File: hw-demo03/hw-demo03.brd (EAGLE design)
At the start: 83.5 x 63.5 mm, 40 parts, among them IC3 MCP2562T, IC4 STM32F042

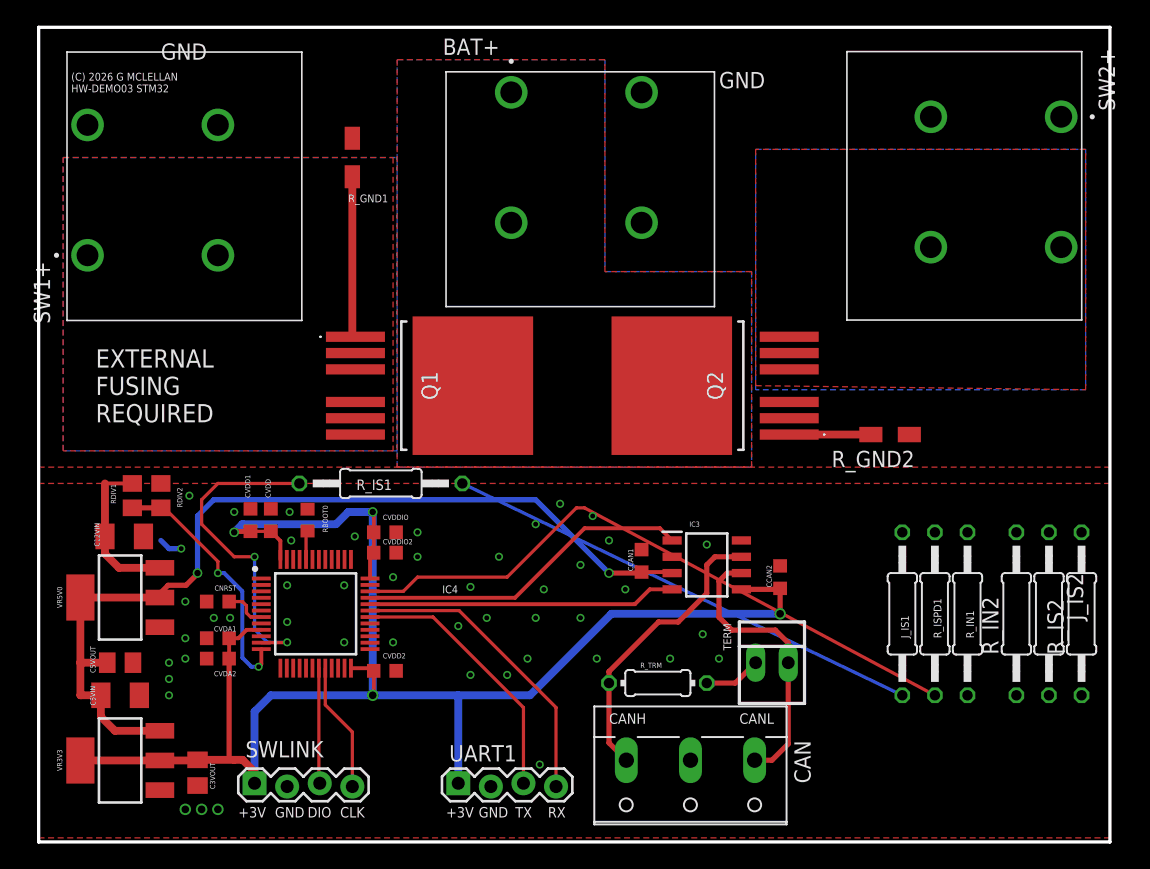
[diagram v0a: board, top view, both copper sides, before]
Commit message: first routing pass completed
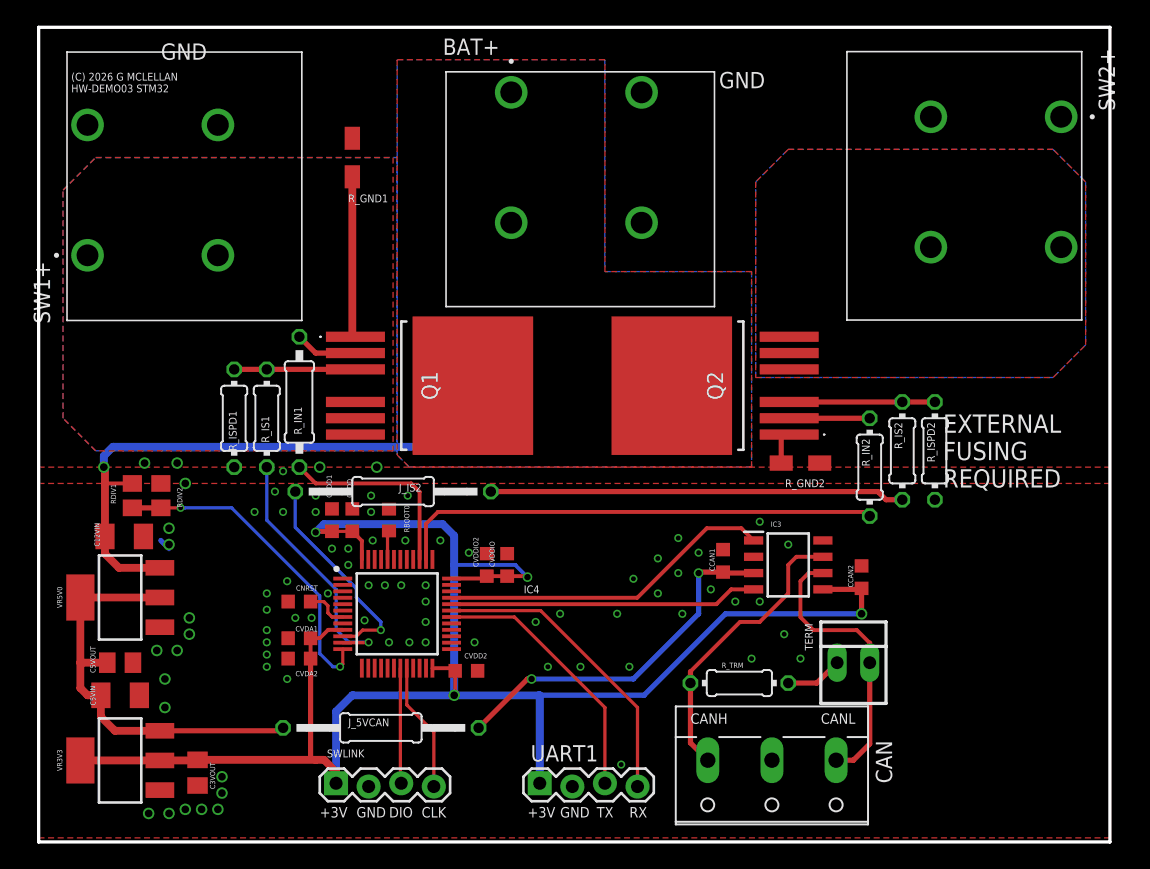
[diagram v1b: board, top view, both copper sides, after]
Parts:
- removed J_IS1: 0R0, rcl:0207/12
- added J_5VCAN: 000, rcl:0207/15
- added R_ISPD2: 1K0, rcl:0204/7
- J_IS2: value 0R0 -> 000; device rcl:0207/12 -> rcl:0207/15
- R_GND2: value 0R0 -> 000
- R_IN1: device rcl:0207/12 -> rcl:0207/10
- R_IN2, R_IS1, R_IS2, R_ISPD1: device rcl:0207/12 -> rcl:0204/7
- moved R_ISPD1 59.1 mm to (16.5, 33.0)
- moved R_IN1 52.2 mm to (21.6, 34.3)
- moved J_IS2 52.0 mm to (28.9, 27.3), turned to 180 degrees
- moved R_IS2 18.9 mm to (68.6, 30.5), turned to 270 degrees
- moved R_IN2 16.2 mm to (66.0, 29.2)
- moved R_IS1 10.2 mm to (19.1, 33.0), turned to 270 degrees
- moved CVDDIO 9.86 mm to (37.8, 21.6), turned to 90 degrees
- moved CVDDIO2 7.99 mm to (36.2, 21.6), turned to 90 degrees
- moved R_GND2 7.33 mm to (60.6, 29.5)
- moved CAN 6.35 mm to (58.4, 5.08)
- moved CCAN1 6.35 mm to (54.6, 21.9)
- moved CCAN2 6.35 mm to (65.4, 20.6)
- moved CVDD 6.35 mm to (25.7, 25.1)
- moved CVDD2 6.35 mm to (34.6, 13.3)
- moved IC4 6.35 mm to (29.2, 17.8)
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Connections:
- net +5V: now also J_5VCAN.2; no longer CCAN1.1, IC3.3
- net ADC3: now also IC4.10, J_IS2.2; no longer R_IS2.2
- net CTL1: no longer IC4.34
- net CTL2: now also IC4.38; no longer IC4.40
- net GND: now also R_ISPD2.1
- net IS: now also R_IS1.1; no longer J_IS1.1
- net N$2: now also J_IS2.1, R_IS2.2; no longer J_IS1.2, R_IS1.1
- net N$6: now also R_IS2.1, R_ISPD2.2; no longer J_IS2.1
- net N$7: now also CCAN1.1, IC3.3, J_5VCAN.1; no longer J_IS2.2, R_IS2.1
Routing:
- net +5V: track 72.6 -> 33.9 mm, vias 2 -> 0
- net CTL2: track 0.00 -> 37.9 mm
- net CTL1: track 50.4 -> 15.4 mm
- net N$7: track 0.00 -> 28.4 mm, vias 0 -> 2
- net +12V: track 12.4 -> 40.3 mm, vias 0 -> 1
- net ADC3: track 0.00 -> 16.7 mm, vias 0 -> 1
- net +3V3: track 129.6 -> 141.3 mm
- net N$6: track 0.00 -> 11.4 mm
- net IS: track 0.00 -> 9.45 mm
- net N$5: track 0.00 -> 6.28 mm
- net ADC1: track 25.9 -> 19.9 mm, vias 2 -> 1
- net ADC2: track 20.0 -> 25.8 mm
- net N$2: track 38.1 -> 32.3 mm
- net CTL3`: track 0.00 -> 4.90 mm
- net N$4: track 6.36 -> 2.84 mm
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
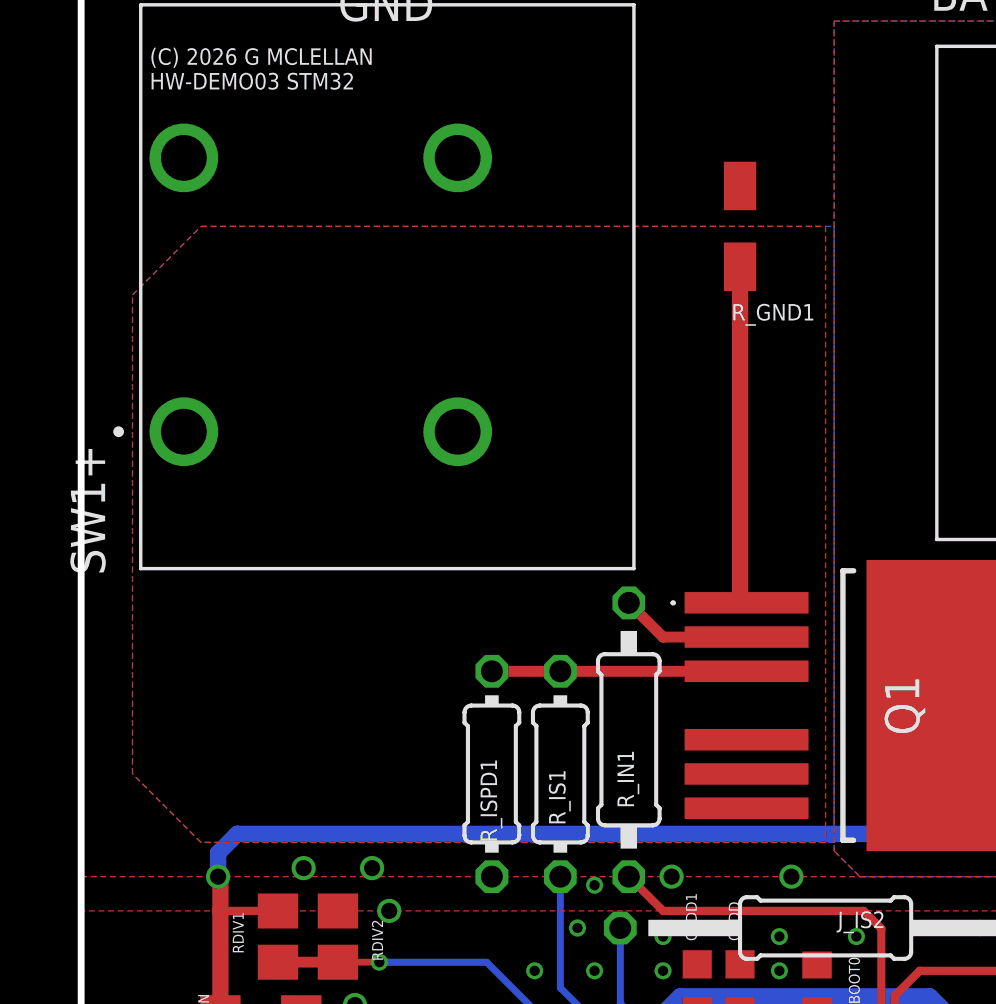
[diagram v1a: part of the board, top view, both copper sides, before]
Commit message: tweak pour for sw1
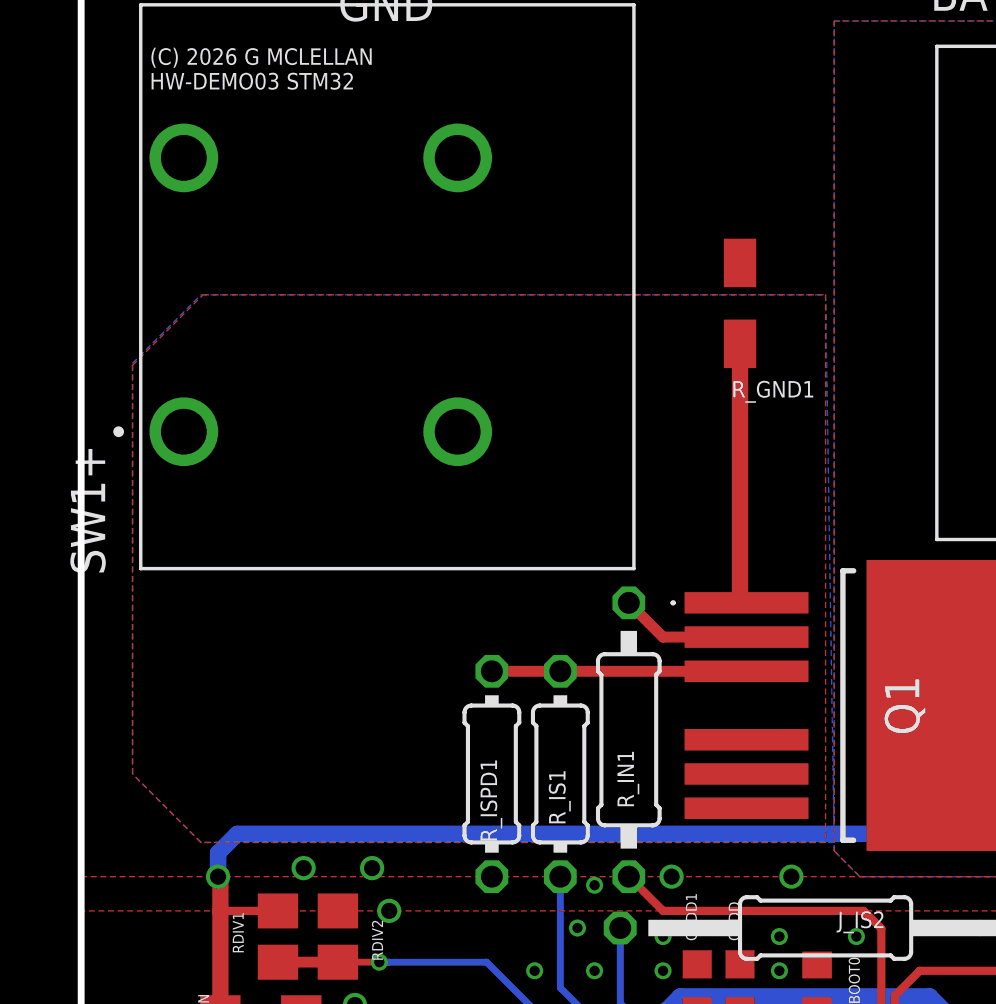
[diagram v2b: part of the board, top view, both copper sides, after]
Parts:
- moved R_GND1 2.86 mm to (25.7, 50.5)
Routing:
- net N$3: track 12.7 -> 9.86 mm
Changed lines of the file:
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@@
 <attribute name="NAME" x="19.2405" y="31.115" size="0.6096" layer="25" ratio="10" rot="R90"/>
 </element>
-<element name="R_GND1" library="rcl" package="R1206W" value="0R0" x="25.7175" y="53.34" smashed="yes" rot="R270">
-<attribute name="NAME" x="25.4" y="49.8475" size="0.6096" layer="25" font="vector" ratio="14"/>
+<element name="R_GND1" library="rcl" package="R1206W" value="0R0" x="25.7175" y="50.4825" smashed="yes" rot="R270">
+<attribute name="NAME" x="25.4" y="46.99" size="0.6096" layer="25" font="vector" ratio="14"/>
 </element>
 <element name="Q1" library="BTS500101TADATMA2" package="BTS500101TADATMA2" value="" x="32.385" y="35.56" rot="R270">
@@
 <polygon width="0.6096" layer="1" thermals="no" rank="4">
 <vertex x="3.175" y="33.02"/>
-<vertex x="3.175" y="50.8"/>
-<vertex x="5.715" y="53.34"/>
-<vertex x="28.8925" y="53.34"/>
+<vertex x="3.175" y="48.181828125"/>
+<vertex x="5.793171875" y="50.8"/>
+<vertex x="28.8925" y="50.8"/>
 <vertex x="28.8925" y="30.48"/>
 <vertex x="5.715" y="30.48"/>
@@
 <polygon width="0.6096" layer="16" rank="4">
 <vertex x="3.175" y="33.02"/>
-<vertex x="3.175" y="50.8"/>
-<vertex x="5.715" y="53.34"/>
-<vertex x="29.21" y="53.34"/>
+<vertex x="3.175" y="48.26"/>
+<vertex x="5.715" y="50.8"/>
+<vertex x="28.8925" y="50.8"/>
 <vertex x="29.21" y="30.48"/>
 <vertex x="5.715" y="30.48"/>
@@
 <contactref element="Q1" pad="1"/>
 <contactref element="R_GND1" pad="2"/>
-<wire x1="25.7175" y1="51.841" x2="25.7175" y2="39.37" width="0.6096" layer="1"/>
+<wire x1="25.7175" y1="48.9835" x2="25.7175" y2="39.37" width="0.6096" layer="1"/>
 <wire x1="25.7175" y1="39.37" x2="25.96" y2="39.37" width="0.6096" layer="1"/>
 </signal>

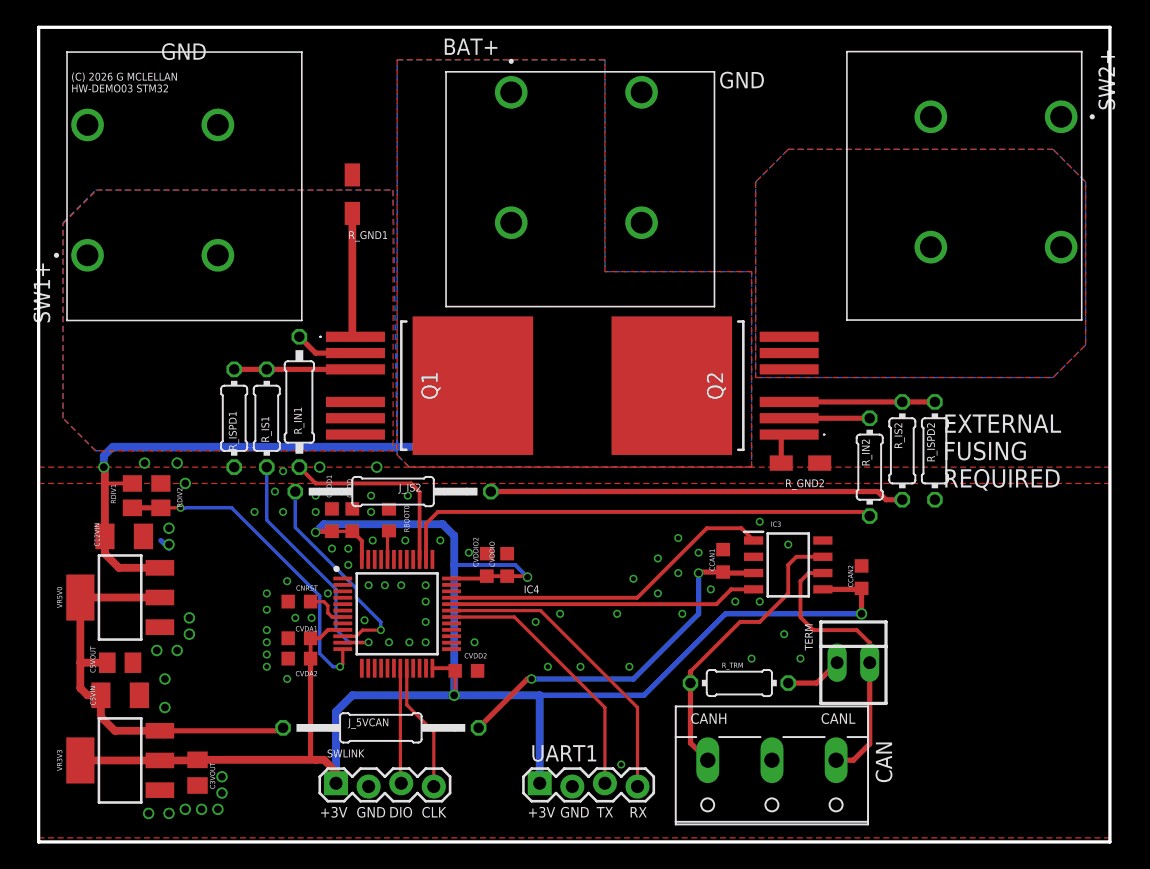
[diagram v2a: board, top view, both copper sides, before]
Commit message: lots of ground plane and power pour stitching
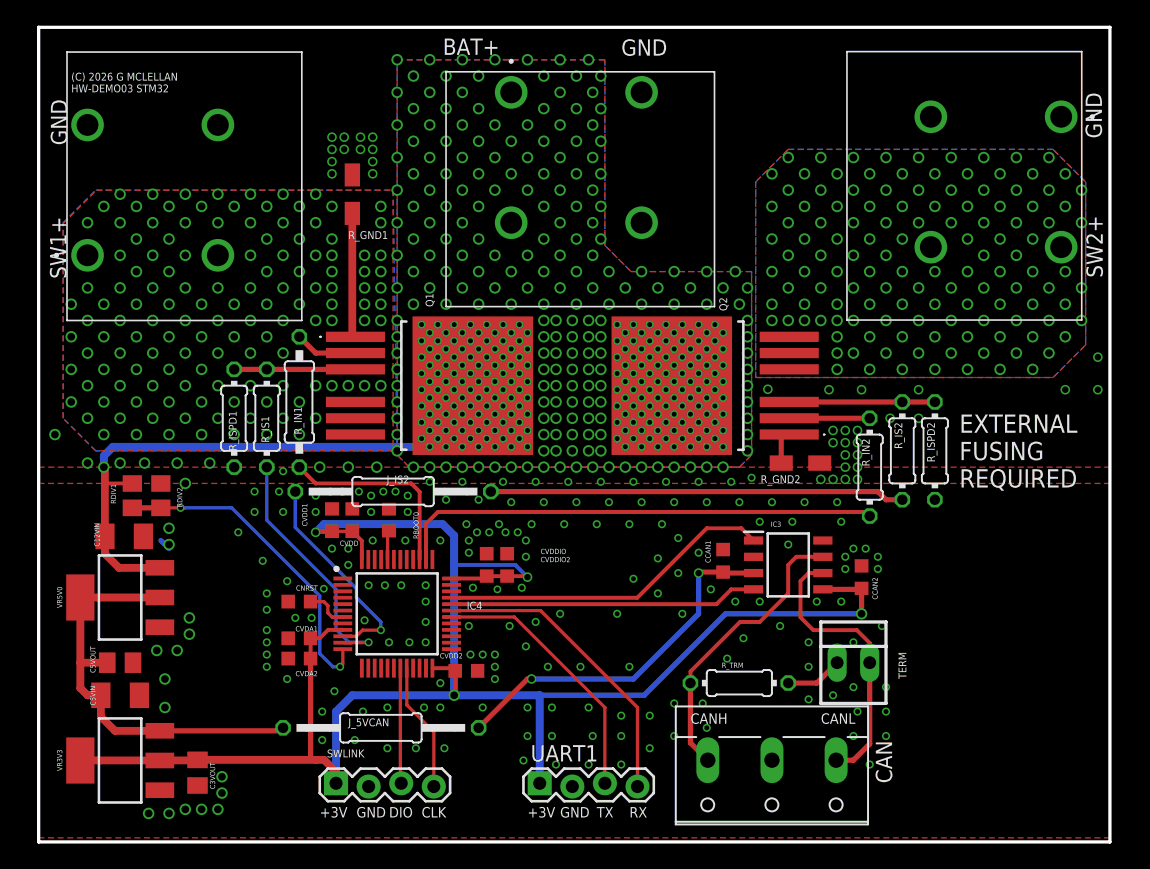
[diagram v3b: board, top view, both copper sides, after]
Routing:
- net GND: vias 80 -> 230
- net +12V: vias 1 -> 425
